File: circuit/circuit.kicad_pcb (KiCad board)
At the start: 2 copper layers, 33 x 33 mm, 3 parts

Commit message: making some improvements to the end circuit
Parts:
- added REF**: Pad_5mm, Pad_5mm, F.Cu at (184.9, 96.0)
- added REF**: Pad_5mm, Pad_5mm, F.Cu at (184.9, 81.8)
- added REF**: Pad_5mm, Pad_5mm, F.Cu at (170.7, 96.0)
- added REF**: Pad_5mm, Pad_5mm, F.Cu at (170.7, 81.8)
- added REF**: MountingHole_2.2mm_M2, MountingHole:MountingHole_2.2mm_M2, F.Cu at (177.8, 74.6)
- added REF**: SolderWirePad_1x01_SMD_5x10mm, Connector_Wire:SolderWirePad_1x01_SMD_5x10mm, F.Cu at (177.8, 99.1)
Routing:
- net VSS: track 0.00 -> 22.7 mm
- net GND: track 0.00 -> 21.6 mm
- added copper zone on F.Cu, net VSS
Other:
- net class power added: clearance 0.2, trace_width 3, via_dia 0.8, via_drill 0.4
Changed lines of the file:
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@@
   (general
     (thickness 1.6)
-    (drawings 1)
-    (tracks 0)
+    (drawings 5)
+    (tracks 8)
     (zones 0)
-    (modules 3)
-    (nets 2)
+    (modules 9)
+    (nets 3)
   )
   (page A4)
@@
     (last_trace_width 0.25)
     (trace_clearance 0.2)
-    (zone_clearance 0.508)
+    (zone_clearance 1)
     (zone_45_only no)
     (trace_min 0.2)
@@
     (mod_text_size 1 1)
     (mod_text_width 0.15)
-    (pad_size 1.524 1.524)
-    (pad_drill 0.762)
+    (pad_size 5 5)
+    (pad_drill 0)
     (pad_to_mask_clearance 0)
     (aux_axis_origin 0 0)
     (visible_elements FFFFFF7F)
     (pcbplotparams
-      (layerselection 0x010fc_ffffffff)
+      (layerselection 0x01000_ffffffff)
       (usegerberextensions false)
       (usegerberattributes true)
@@
       (outputformat 1)
       (mirror false)
-      (drillshape 1)
+      (drillshape 0)
       (scaleselection 1)
-      (outputdirectory ""))
+      (outputdirectory "output_files/"))
   )
   (net 0 "")
   (net 1 GND)
+  (net 2 VSS)
   (net_class Default "This is the default net class."
     (clearance 0.2)
@@
     (uvia_dia 0.3)
     (uvia_drill 0.1)
+  )
+  (net_class power ""
+    (clearance 0.2)
+    (trace_width 3)
+    (via_dia 0.8)
+    (via_drill 0.4)
+    (uvia_dia 0.3)
+    (uvia_drill 0.1)
     (add_net GND)
+    (add_net VSS)
+  )
+  (module Pad_5mm (layer F.Cu)
+    (at 184.95 96.05)
+    (fp_text reference REF** (at 0 0.5) (layer F.SilkS)
+      (effects (font (size 1 1) (thickness 0.15)))
+    )
+    (fp_text value Pad_5mm (at 0 -0.5) (layer F.Fab)
+      (effects (font (size 1 1) (thickness 0.15)))
+    )
+    (pad 1 smd circle (at 0 0) (size 5 5) (layers F.Cu F.Paste F.Mask)
+      (net 1 GND))
+  )
+  (module Pad_5mm (layer F.Cu)
+    (at 184.95 81.75)
+    (fp_text reference REF** (at 0 0.5) (layer F.SilkS)
+      (effects (font (size 1 1) (thickness 0.15)))
+    )
+    (fp_text value Pad_5mm (at 0 -0.5) (layer F.Fab)
+      (effects (font (size 1 1) (thickness 0.15)))
+    )
+    (pad 1 smd circle (at 0 0) (size 5 5) (layers F.Cu F.Paste F.Mask)
+      (net 1 GND))
+  )
+  (module Pad_5mm (layer F.Cu)
+    (at 170.65 96.05)
+    (fp_text reference REF** (at 0 0.5) (layer F.SilkS)
+      (effects (font (size 1 1) (thickness 0.15)))
+    )
+    (fp_text value Pad_5mm (at 0 -0.5) (layer F.Fab)
+      (effects (font (size 1 1) (thickness 0.15)))
+    )
+    (pad 1 smd circle (at 0 0) (size 5 5) (layers F.Cu F.Paste F.Mask)
+      (net 2 VSS))
+  )
+  (module Pad_5mm (layer F.Cu)
+    (at 170.65 81.75)
+    (fp_text reference REF** (at 0 0.5) (layer F.SilkS)
+      (effects (font (size 1 1) (thickness 0.15)))
+    )
+    (fp_text value Pad_5mm (at 0 -0.5) (layer F.Fab)
+      (effects (font (size 1 1) (thickness 0.15)))
+    )
+    (pad 1 smd circle (at 0 0) (size 5 5) (layers F.Cu F.Paste F.Mask)
+      (net 2 VSS))
+  )
+  (module MountingHole:MountingHole_2.2mm_M2 (layer F.Cu)
+    (at 177.8 74.6276)
+    (descr "Mounting Hole 2.2mm, no annular, M2")
+    (tags "mounting hole 2.2mm no annular m2")
+    (attr virtual)
+    (fp_text reference REF** (at 0 -3.2) (layer F.SilkS)
+      (effects (font (size 1 1) (thickness 0.15)))
+    )
+    (fp_text value MountingHole_2.2mm_M2 (at 0 3.2) (layer F.Fab)
+      (effects (font (size 1 1) (thickness 0.15)))
+    )
+    (fp_text user %R (at 0.3 0) (layer F.Fab)
+      (effects (font (size 1 1) (thickness 0.15)))
+    )
+    (fp_circle (center 0 0) (end 2.2 0) (layer Cmts.User) (width 0.15))
+    (fp_circle (center 0 0) (end 2.45 0) (layer F.CrtYd) (width 0.05))
+    (pad 1 np_thru_hole circle (at 0 0) (size 2.2 2.2) (drill 2.2) (layers *.Cu *.Mask))
+  )
+  (module Connector_Wire:SolderWirePad_1x01_SMD_5x10mm (layer F.Cu)
+    (at 177.8 99.06)
+    (descr "Wire Pad, Square, SMD Pad,  5mm x 10mm,")
+    (tags "MesurementPoint Square SMDPad 5mmx10mm ")
+    (attr smd virtual)
+    (fp_text reference REF** (at 0 -3.81) (layer F.SilkS)
+      (effects (font (size 1 1) (thickness 0.15)))
+    )
+    (fp_text value SolderWirePad_1x01_SMD_5x10mm (at 0 6.35) (layer F.Fab)
+      (effects (font (size 1 1) (thickness 0.15)))
+    )
+    (fp_text user %R (at 0 0) (layer F.Fab)
+      (effects (font (size 1 1) (thickness 0.15)))
+    )
+    (fp_line (start 2.75 -5.25) (end -2.75 -5.25) (layer F.CrtYd) (width 0.05))
+    (fp_line (start 2.75 5.25) (end 2.75 -5.25) (layer F.CrtYd) (width 0.05))
+    (fp_line (start -2.75 5.25) (end 2.75 5.25) (layer F.CrtYd) (width 0.05))
+    (fp_line (start -2.75 -5.25) (end -2.75 5.25) (layer F.CrtYd) (width 0.05))
+    (pad 1 smd rect (at 0 0) (size 5 10) (layers F.Cu F.Paste F.Mask)
+      (net 2 VSS))
   )
   (module MountingHole:MountingHole_2.2mm_M2 (layer F.Cu)
@@
       (effects (font (size 1 1) (thickness 0.15)))
     )
+    (fp_circle (center 0 0) (end 2.45 0) (layer F.CrtYd) (width 0.05))
+    (fp_circle (center 0 0) (end 2.2 0) (layer Cmts.User) (width 0.15))
     (fp_text user %R (at 2.8424 0) (layer F.Fab)
       (effects (font (size 1 1) (thickness 0.15)))
     )
-    (fp_circle (center 0 0) (end 2.2 0) (layer Cmts.User) (width 0.15))
-    (fp_circle (center 0 0) (end 2.45 0) (layer F.CrtYd) (width 0.05))
     (pad 1 np_thru_hole circle (at 0 0) (size 2.2 2.2) (drill 2.2) (layers *.Cu *.Mask))
   )
@@
       (effects (font (size 1 1) (thickness 0.15)))
     )
+    (fp_circle (center 0 0) (end 2.45 0) (layer F.CrtYd) (width 0.05))
+    (fp_circle (center 0 0) (end 2.2 0) (layer Cmts.User) (width 0.15))
     (fp_text user %R (at 0.3 0) (layer F.Fab)
       (effects (font (size 1 1) (thickness 0.15)))
     )
-    (fp_circle (center 0 0) (end 2.2 0) (layer Cmts.User) (width 0.15))
-    (fp_circle (center 0 0) (end 2.45 0) (layer F.CrtYd) (width 0.05))
     (pad 1 np_thru_hole circle (at 0 0) (size 2.2 2.2) (drill 2.2) (layers *.Cu *.Mask))
   )
@@
       (effects (font (size 1 1) (thickness 0.15)))
     )
+    (fp_circle (center 0 0) (end 3.05 0) (layer F.CrtYd) (width 0.05))
+    (fp_circle (center 0 0) (end 2.8 0) (layer Cmts.User) (width 0.15))
     (fp_text user %R (at 0.3 0) (layer F.Fab)
       (effects (font (size 1 1) (thickness 0.15)))
     )
-    (fp_circle (center 0 0) (end 2.8 0) (layer Cmts.User) (width 0.15))
-    (fp_circle (center 0 0) (end 3.05 0) (layer F.CrtYd) (width 0.05))
     (pad 1 connect circle (at 0 0) (size 5.6 5.6) (layers B.Cu B.Mask)
       (net 1 GND))
@@
       (net 1 GND))
   )
+  (gr_circle (center 170.65 96.05) (end 175.65 96.05) (layer Dwgs.User) (width 0.15))
+  (gr_circle (center 170.65 81.75) (end 175.65 81.75) (layer Dwgs.User) (width 0.15))
+  (gr_circle (center 184.95 81.75) (end 189.95 81.75) (layer Dwgs.User) (width 0.15))
+  (gr_circle (center 184.95 96.05) (end 189.95 96.05) (layer Dwgs.User) (width 0.15))
   (gr_circle (center 177.8 88.9) (end 194.3 88.9) (layer Edge.Cuts) (width 0.05))
+  (segment (start 184.48 88.9) (end 184.95 88.43) (width 3) (layer F.Cu) (net 1))
+  (segment (start 177.8 88.9) (end 184.48 88.9) (width 3) (layer F.Cu) (net 1))
+  (segment (start 184.95 88.43) (end 184.95 96.05) (width 3) (layer F.Cu) (net 1))
+  (segment (start 184.95 81.75) (end 184.95 88.43) (width 3) (layer F.Cu) (net 1))
+  (segment (start 170.65 81.75) (end 170.65 88.43) (width 3) (layer F.Cu) (net 2))
+  (segment (start 170.65 88.43) (end 170.65 96.05) (width 3) (layer F.Cu) (net 2))
+  (segment (start 173.66 99.06) (end 170.65 96.05) (width 3) (layer F.Cu) (net 2))
+  (segment (start 177.8 99.06) (end 173.66 99.06) (width 3) (layer F.Cu) (net 2))
   (zone (net 1) (net_name GND) (layer F.Cu) (hatch edge 0.508)
-    (connect_pads yes (clearance 0.508))
+    (priority 1)
+    (connect_pads no (clearance 1))
     (min_thickness 1)
-    (fill yes (arc_segments 32) (thermal_gap 0.508) (thermal_bridge_width 2))
+    (fill yes (arc_segments 32) (thermal_gap 1) (thermal_bridge_width 3))
     (polygon
       (pts
-        (xy 195.58 106.68) (xy 177.8 106.68) (xy 177.8 71.12) (xy 195.58 71.12)
+        (xy 195.58 106.68) (xy 178.435 106.68) (xy 178.435 71.12) (xy 195.58 71.12)
       )
     )
+  )
+  (zone (net 2) (net_name VSS) (layer F.Cu) (hatch edge 0.508)
+    (priority 1)
+    (connect_pads no (clearance 1))
+    (min_thickness 1)
+    (fill yes (arc_segments 32) (thermal_gap 1) (thermal_bridge_width 3))
+    (polygon
+      (pts
+        (xy 177.165 106.68) (xy 160.02 106.68) (xy 160.02 71.12) (xy 177.165 71.12)
+      )
+    )

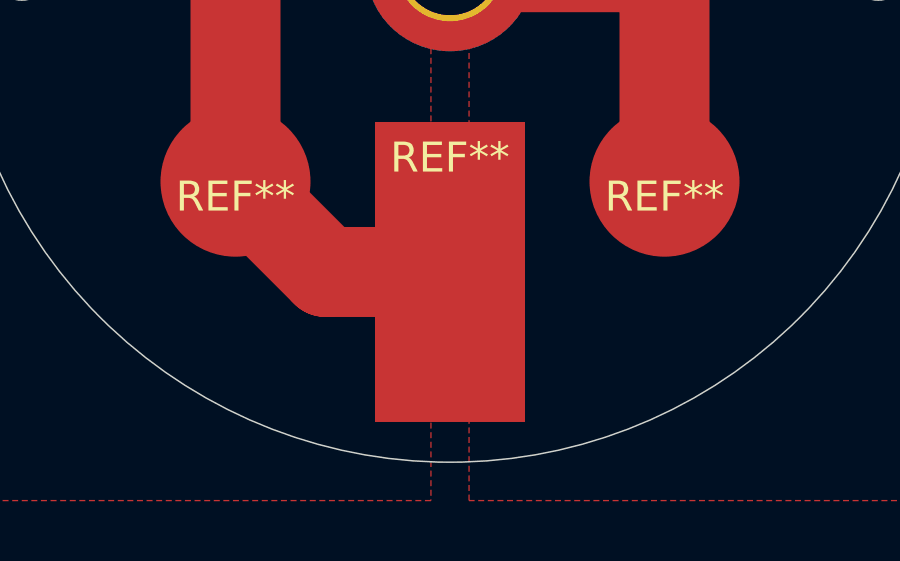
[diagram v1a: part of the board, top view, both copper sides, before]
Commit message: adding an optional header pin hole that can be drilled so we dont have to solder
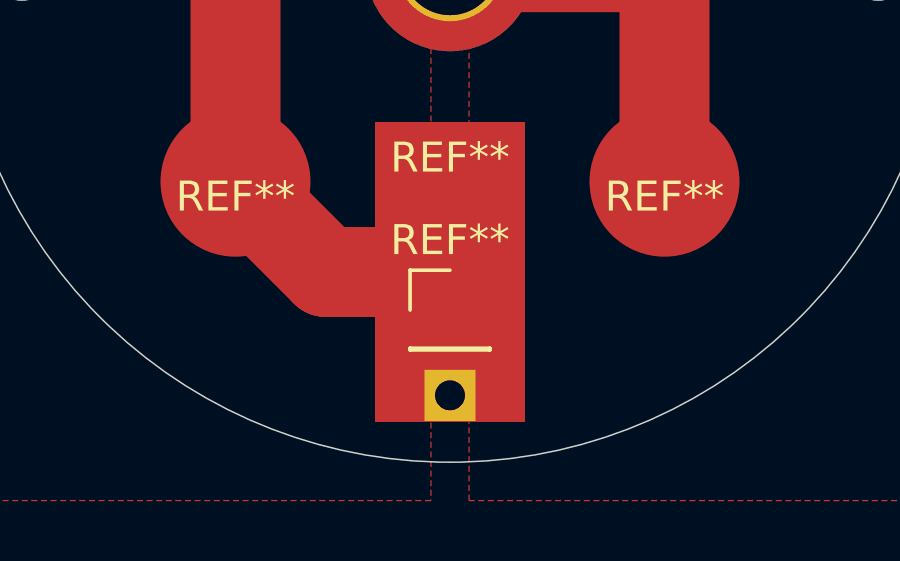
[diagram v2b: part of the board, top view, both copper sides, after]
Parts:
- added REF**: PinHeader_1x01_P2.54mm_Vertical, Connector_PinHeader_2.54mm:PinHeader_1x01_P2.54mm_Vertical, F.Cu at (177.8, 100.3)
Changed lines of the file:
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@@
     (tracks 8)
     (zones 0)
-    (modules 9)
+    (modules 10)
     (nets 3)
   )
@@
     (mod_text_size 1 1)
     (mod_text_width 0.15)
-    (pad_size 5 5)
-    (pad_drill 0)
+    (pad_size 1.7 1.7)
+    (pad_drill 1)
     (pad_to_mask_clearance 0)
     (aux_axis_origin 0 0)
@@
     (add_net VSS)
   )
+  (module Connector_PinHeader_2.54mm:PinHeader_1x01_P2.54mm_Vertical (layer F.Cu)
+    (at 177.8 100.33)
+    (descr "Through hole straight pin header, 1x01, 2.54mm pitch, single row")
+    (tags "Through hole pin header THT 1x01 2.54mm single row")
+    (fp_text reference REF** (at 0 -2.33) (layer F.SilkS)
+      (effects (font (size 1 1) (thickness 0.15)))
+    )
+    (fp_text value PinHeader_1x01_P2.54mm_Vertical (at 0 2.33) (layer F.Fab)
+      (effects (font (size 1 1) (thickness 0.15)))
+    )
+    (fp_text user %R (at 0 0 90) (layer F.Fab)
+      (effects (font (size 1 1) (thickness 0.15)))
+    )
+    (fp_line (start -0.635 -1.27) (end 1.27 -1.27) (layer F.Fab) (width 0.1))
+    (fp_line (start 1.27 -1.27) (end 1.27 1.27) (layer F.Fab) (width 0.1))
+    (fp_line (start 1.27 1.27) (end -1.27 1.27) (layer F.Fab) (width 0.1))
+    (fp_line (start -1.27 1.27) (end -1.27 -0.635) (layer F.Fab) (width 0.1))
+    (fp_line (start -1.27 -0.635) (end -0.635 -1.27) (layer F.Fab) (width 0.1))
+    (fp_line (start -1.33 1.33) (end 1.33 1.33) (layer F.SilkS) (width 0.12))
+    (fp_line (start -1.33 1.27) (end -1.33 1.33) (layer F.SilkS) (width 0.12))
+    (fp_line (start 1.33 1.27) (end 1.33 1.33) (layer F.SilkS) (width 0.12))
+    (fp_line (start -1.33 1.27) (end 1.33 1.27) (layer F.SilkS) (width 0.12))
+    (fp_line (start -1.33 0) (end -1.33 -1.33) (layer F.SilkS) (width 0.12))
+    (fp_line (start -1.33 -1.33) (end 0 -1.33) (layer F.SilkS) (width 0.12))
+    (fp_line (start -1.8 -1.8) (end -1.8 1.8) (layer F.CrtYd) (width 0.05))
+    (fp_line (start -1.8 1.8) (end 1.8 1.8) (layer F.CrtYd) (width 0.05))
+    (fp_line (start 1.8 1.8) (end 1.8 -1.8) (layer F.CrtYd) (width 0.05))
+    (fp_line (start 1.8 -1.8) (end -1.8 -1.8) (layer F.CrtYd) (width 0.05))
+    (pad 1 thru_hole rect (at 0 2.8424) (size 1.7 1.7) (drill 1) (layers *.Cu *.Mask)
+      (net 2 VSS))
+    (model ${KISYS3DMOD}/Connector_PinHeader_2.54mm.3dshapes/PinHeader_1x01_P2.54mm_Vertical.wrl
+      (at (xyz 0 0 0))
+      (scale (xyz 1 1 1))
+      (rotate (xyz 0 0 0))
+    )
+  )
   (module Pad_5mm (layer F.Cu)
     (at 184.95 96.05)
@@
       (effects (font (size 1 1) (thickness 0.15)))
     )
+    (fp_circle (center 0 0) (end 2.45 0) (layer F.CrtYd) (width 0.05))
+    (fp_circle (center 0 0) (end 2.2 0) (layer Cmts.User) (width 0.15))
     (fp_text user %R (at 0.3 0) (layer F.Fab)
       (effects (font (size 1 1) (thickness 0.15)))
     )
-    (fp_circle (center 0 0) (end 2.2 0) (layer Cmts.User) (width 0.15))
-    (fp_circle (center 0 0) (end 2.45 0) (layer F.CrtYd) (width 0.05))
     (pad 1 np_thru_hole circle (at 0 0) (size 2.2 2.2) (drill 2.2) (layers *.Cu *.Mask))
   )
@@
       (effects (font (size 1 1) (thickness 0.15)))
     )
+    (fp_line (start -2.75 -5.25) (end -2.75 5.25) (layer F.CrtYd) (width 0.05))
+    (fp_line (start -2.75 5.25) (end 2.75 5.25) (layer F.CrtYd) (width 0.05))
+    (fp_line (start 2.75 5.25) (end 2.75 -5.25) (layer F.CrtYd) (width 0.05))
+    (fp_line (start 2.75 -5.25) (end -2.75 -5.25) (layer F.CrtYd) (width 0.05))
     (fp_text user %R (at 0 0) (layer F.Fab)
       (effects (font (size 1 1) (thickness 0.15)))
     )
-    (fp_line (start 2.75 -5.25) (end -2.75 -5.25) (layer F.CrtYd) (width 0.05))
-    (fp_line (start 2.75 5.25) (end 2.75 -5.25) (layer F.CrtYd) (width 0.05))
-    (fp_line (start -2.75 5.25) (end 2.75 5.25) (layer F.CrtYd) (width 0.05))
-    (fp_line (start -2.75 -5.25) (end -2.75 5.25) (layer F.CrtYd) (width 0.05))
     (pad 1 smd rect (at 0 0) (size 5 10) (layers F.Cu F.Paste F.Mask)
       (net 2 VSS))
@@
       (effects (font (size 1 1) (thickness 0.15)))
     )
+    (fp_circle (center 0 0) (end 2.2 0) (layer Cmts.User) (width 0.15))
     (fp_circle (center 0 0) (end 2.45 0) (layer F.CrtYd) (width 0.05))
-    (fp_circle (center 0 0) (end 2.2 0) (layer Cmts.User) (width 0.15))
     (fp_text user %R (at 2.8424 0) (layer F.Fab)
       (effects (font (size 1 1) (thickness 0.15)))
@@
       (effects (font (size 1 1) (thickness 0.15)))
     )
+    (fp_circle (center 0 0) (end 2.2 0) (layer Cmts.User) (width 0.15))
     (fp_circle (center 0 0) (end 2.45 0) (layer F.CrtYd) (width 0.05))
-    (fp_circle (center 0 0) (end 2.2 0) (layer Cmts.User) (width 0.15))
     (fp_text user %R (at 0.3 0) (layer F.Fab)
       (effects (font (size 1 1) (thickness 0.15)))
@@
       (effects (font (size 1 1) (thickness 0.15)))
     )
+    (fp_circle (center 0 0) (end 2.8 0) (layer Cmts.User) (width 0.15))
     (fp_circle (center 0 0) (end 3.05 0) (layer F.CrtYd) (width 0.05))
-    (fp_circle (center 0 0) (end 2.8 0) (layer Cmts.User) (width 0.15))
     (fp_text user %R (at 0.3 0) (layer F.Fab)
       (effects (font (size 1 1) (thickness 0.15)))
